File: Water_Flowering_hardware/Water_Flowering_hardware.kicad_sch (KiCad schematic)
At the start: 14 parts, among them J1 Water_Level_Sensor_Module, J2 Soil_Moisture_Sensor_Module, J3 Conn_01x02, J4 Power Jack, K1 Relay_SPDT, Q1 MMBT5550L, U1 CD74HC4067SM, U2 WeMos_D1_mini

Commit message: Fix: 修正JACK的VIN和GND腳位和走線和修正5V的走線
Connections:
- net GND: now also J4.2 (Pin_2); no longer J4.1 (Pin_1)
- net VIN: now also J4.1 (Pin_1); no longer J4.2 (Pin_2)
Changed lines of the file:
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@@
 	)
 	(label "VIN"
-		(at 114.9604 169.4942 180)
+		(at 120.65 166.37 180)
 		(fields_autoplaced yes)
 		(effects
@@
 		)
 	)
+	(label "GND"
+		(at 120.65 171.45 180)
+		(fields_autoplaced yes)
+		(effects
+			(font
+				(size 1.27 1.27)
+			)
+			(justify right bottom)
+		)
+	)
 	(label "Soil_D0"
 		(at 168.91 88.9 0)
@@
 		)
 	)
-	(label "GND"
-		(at 114.9604 172.0342 180)
-		(fields_autoplaced yes)
-		(effects
-			(font
-				(size 1.27 1.27)
-			)
-			(justify right bottom)
-		)
-	)
 	(label "W0"
 		(at 168.91 91.44 0)
@@
 	)
 	(label "GND"
-		(at 114.9604 166.9542 180)
+		(at 120.65 168.91 180)
 		(fields_autoplaced yes)
 		(effects
@@
 			)
 			(justify right bottom)
+		)
+	)
+	(symbol
+		(lib_id "Connector:Conn_01x03_Socket")
+		(at 125.73 168.91 0)
+		(unit 1)
+		(exclude_from_sim no)
+		(in_bom yes)
+		(on_board yes)
+		(dnp no)
+		(property "Reference" "J4"
+			(at 121.92 162.56 0)
+			(effects
+				(font
+					(size 1.27 1.27)
+				)
+				(justify left)
+			)
+		)
+		(property "Value" "Power Jack"
+			(at 114.3 173.99 0)
+			(effects
+				(font
+					(size 1.27 1.27)
+				)
+				(justify left)
+			)
+		)
+		(property "Footprint" "Connector_BarrelJack:BarrelJack_GCT_DCJ200-10-A_Horizontal"
+			(at 125.73 168.91 0)
+			(effects
+				(font
+					(size 1.27 1.27)
+				)
+				(hide yes)
+			)
+		)
+		(property "Datasheet" "~"
+			(at 125.73 168.91 0)
+			(effects
+				(font
+					(size 1.27 1.27)
+				)
+				(hide yes)
+			)
+		)
+		(property "Description" ""
+			(at 125.73 168.91 0)
+			(effects
+				(font
+					(size 1.27 1.27)
+				)
+				(hide yes)
+			)
+		)
+		(pin "1"
+		)
+		(pin "2"
+		)
+		(pin "3"
+		)
+		(instances
+			(project "Water_Flowering_hardware"
+				(path "/2430d23c-7a32-4c0f-92aa-bc816bceade1"
+					(reference "J4")
+					(unit 1)
+				)
+			)
 		)
 	)
@@
 					(unit 1)
 				)
-			)
-		)
-	)
-	(symbol
-		(lib_id "Connector:Conn_01x03_Socket")
-		(at 120.0404 169.4942 0)
-		(unit 1)
-		(exclude_from_sim no)
-		(in_bom yes)
-		(on_board yes)
-		(dnp no)
-		(property "Reference" "J4"
-			(at 116.2304 163.1442 0)
-			(effects
-				(font
-					(size 1.27 1.27)
-				)
-				(justify left)
-			)
-		)
-		(property "Value" "Power Jack"
-			(at 108.6104 174.5742 0)
-			(effects
-				(font
-					(size 1.27 1.27)
-				)
-				(justify left)
-			)
-		)
-		(property "Footprint" "Connector_BarrelJack:BarrelJack_GCT_DCJ200-10-A_Horizontal"
-			(at 120.0404 169.4942 0)
-			(effects
-				(font
-					(size 1.27 1.27)
-				)
-				(hide yes)
-			)
-		)
-		(property "Datasheet" "~"
-			(at 120.0404 169.4942 0)
-			(effects
-				(font
-					(size 1.27 1.27)
-				)
-				(hide yes)
-			)
-		)
-		(property "Description" ""
-			(at 120.0404 169.4942 0)
-			(effects
-				(font
-					(size 1.27 1.27)
-				)
-				(hide yes)
-			)
-		)
-		(pin "1"
-		)
-		(pin "2"
-		)
-		(pin "3"
-		)
-		(instances
-			(project "Water_Flowering_hardware"
-				(path "/2430d23c-7a32-4c0f-92aa-bc816bceade1"
-					(reference "J4")
-					(unit 1)
-				)

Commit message: Fix: 確認CD74HC4067功能後並修正相對的GPIO腳位
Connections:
- net S4 is gone; now on net S3: U2.13 (SDA/D2)
- net S0: now also U2.4 (SCK/D5); no longer U2.16 (TX)
- net S1: now also U2.5 (MISO/D6); no longer U2.15 (RX)
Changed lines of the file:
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@@
 	)
 	(label "S0"
-		(at 184.15 102.87 180)
-		(fields_autoplaced yes)
-		(effects
-			(font
-				(size 1.27 1.27)
-			)
-			(justify right bottom)
+		(at 204.47 105.41 0)
+		(fields_autoplaced yes)
+		(effects
+			(font
+				(size 1.27 1.27)
+			)
+			(justify left bottom)
 		)
 	)
@@
 		)
 	)
-	(label "S4"
+	(label "S3"
 		(at 204.47 97.79 0)
 		(fields_autoplaced yes)
@@
 	)
 	(label "S1"
-		(at 184.15 100.33 180)
-		(fields_autoplaced yes)
-		(effects
-			(font
-				(size 1.27 1.27)
-			)
-			(justify right bottom)
-		)
-	)
+		(at 204.47 107.95 0)
+		(fields_autoplaced yes)
+		(effects
+			(font
+				(size 1.27 1.27)
+			)
+			(justify left bottom)
+		)
+	)

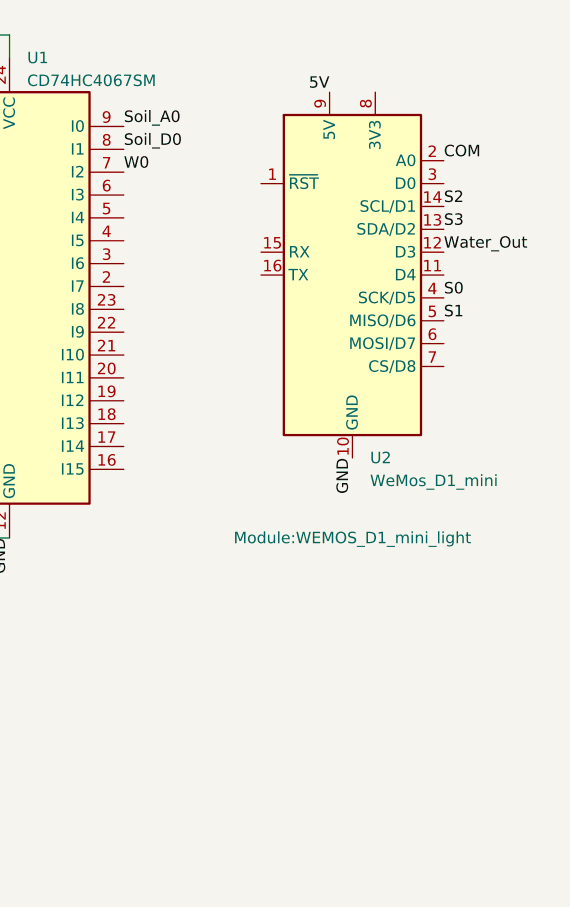
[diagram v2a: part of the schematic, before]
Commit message: Feat: 加入APSTA腳位到D0腳位 - 原本為pull high可進入一種模式(STA或AP)，可透過短路2PIN接地進入另一種模式
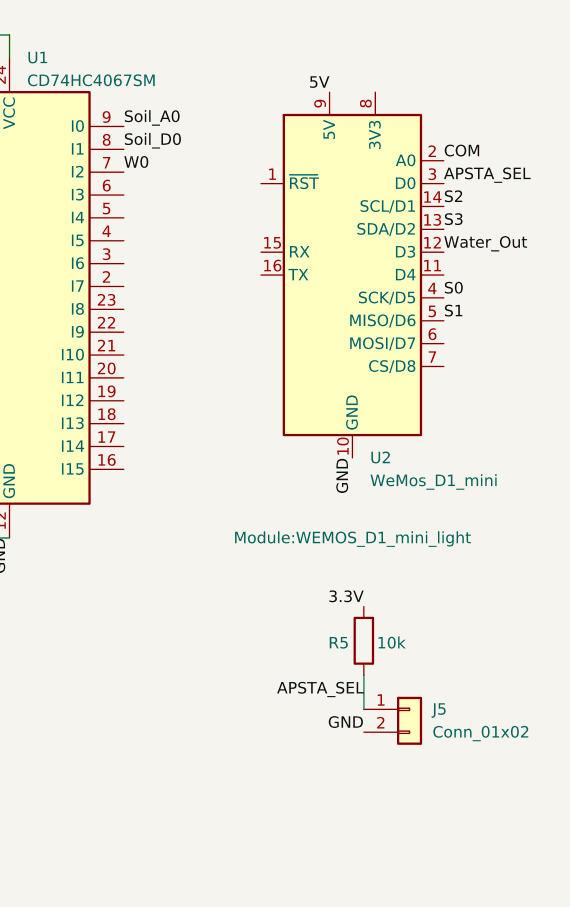
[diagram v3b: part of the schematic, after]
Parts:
- added J5: Conn_01x02, Connector_PinSocket_2.54mm:PinSocket_1x02_P2.54mm_Vertical, symbol Connector_Generic:Conn_01x02
- added R5: 10k, Resistor_SMD:R_0603_1608Metric, symbol Device:R
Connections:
- net 3.3V: now also R5.2
- net GND: now also J5.2 (Pin_2)
- net APSTA_SEL: now reaches U2.3 (D0)
- net APSTA_SEL: now also J5.1 (Pin_1), R5.1
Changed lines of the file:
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@@
+	(wire
+		(pts
+			(xy 195.58 147.32) (xy 195.58 151.13)
+		)
+		(stroke
+			(width 0)
+			(type default)
+		)
+	)
 	(wire
 		(pts
@@
 		)
 	)
+	(label "APSTA_SEL"
+		(at 195.58 149.86 180)
+		(fields_autoplaced yes)
+		(effects
+			(font
+				(size 1.27 1.27)
+			)
+			(justify right bottom)
+		)
+	)
+	(label "GND"
+		(at 195.58 153.67 180)
+		(fields_autoplaced yes)
+		(effects
+			(font
+				(size 1.27 1.27)
+			)
+			(justify right bottom)
+		)
+	)
 	(label "GND"
 		(at 156.21 132.08 270)
@@
 		)
 	)
+	(label "APSTA_SEL"
+		(at 204.47 92.71 0)
+		(fields_autoplaced yes)
+		(effects
+			(font
+				(size 1.27 1.27)
+			)
+			(justify left bottom)
+		)
+	)
 	(label "S3"
 		(at 204.47 97.79 0)
@@
 			)
 			(justify left bottom)
+		)
+	)
+	(label "3.3V"
+		(at 195.58 139.7 180)
+		(fields_autoplaced yes)
+		(effects
+			(font
+				(size 1.27 1.27)
+			)
+			(justify right bottom)
 		)
 	)
@@
 	)
 	(symbol
+		(lib_id "Device:R")
+		(at 195.58 143.51 180)
+		(unit 1)
+		(exclude_from_sim no)
+		(in_bom yes)
+		(on_board yes)
+		(dnp no)
+		(property "Reference" "R5"
+			(at 192.786 143.764 0)
+			(effects
+				(font
+					(size 1.27 1.27)
+				)
+			)
+		)
+		(property "Value" "10k"
+			(at 198.628 143.764 0)
+			(effects
+				(font
+					(size 1.27 1.27)
+				)
+			)
+		)
+		(property "Footprint" "Resistor_SMD:R_0603_1608Metric"
+			(at 197.358 143.51 90)
+			(effects
+				(font
+					(size 1.27 1.27)
+				)
+				(hide yes)
+			)
+		)
+		(property "Datasheet" "~"
+			(at 195.58 143.51 0)
+			(effects
+				(font
+					(size 1.27 1.27)
+				)
+				(hide yes)
+			)
+		)
+		(property "Description" "Resistor"
+			(at 195.58 143.51 0)
+			(effects
+				(font
+					(size 1.27 1.27)
+				)
+				(hide yes)
+			)
+		)
+		(pin "1"
+		)
+		(pin "2"
+		)
+		(instances
+			(project "Water_Flowering_hardware"
+				(path "/2430d23c-7a32-4c0f-92aa-bc816bceade1"
+					(reference "R5")
+					(unit 1)
+				)
+			)
+		)
+	)
+	(symbol
 		(lib_id "Device:D")
 		(at 54.61 52.07 270)
@@
 					(unit 1)
 				)
+			)
+		)
+	)
+	(symbol
+		(lib_id "Connector_Generic:Conn_01x02")
+		(at 200.66 151.13 0)
+		(unit 1)
+		(exclude_from_sim no)
+		(in_bom yes)
+		(on_board yes)
+		(dnp no)
+		(fields_autoplaced yes)
+		(property "Reference" "J5"
+			(at 203.2 151.1299 0)
+			(effects
+				(font
+					(size 1.27 1.27)
+				)
+				(justify left)
+			)
+		)
+		(property "Value" "Conn_01x02"
+			(at 203.2 153.6699 0)
+			(effects
+				(font
+					(size 1.27 1.27)
+				)
+				(justify left)
+			)
+		)
+		(property "Footprint" "Connector_PinSocket_2.54mm:PinSocket_1x02_P2.54mm_Vertical"
+			(at 200.66 151.13 0)
+			(effects
+				(font
+					(size 1.27 1.27)
+				)
+				(hide yes)
+			)
+		)
+		(property "Datasheet" "~"
+			(at 200.66 151.13 0)
+			(effects
+				(font
+					(size 1.27 1.27)
+				)
+				(hide yes)
+			)
+		)
+		(property "Description" "Generic connector, single row, 01x02, script generated (kicad-library-utils/schlib/autogen/connector/)"
+			(at 200.66 151.13 0)
+			(effects
+				(font
+					(size 1.27 1.27)
+				)
+				(hide yes)
+			)
+		)
+		(pin "2"
+		)
+		(pin "1"
+		)
+		(instances
+			(project "Water_Flowering_hardware"
+				(path "/2430d23c-7a32-4c0f-92aa-bc816bceade1"
+					(reference "J5")
+					(unit 1)
+				)

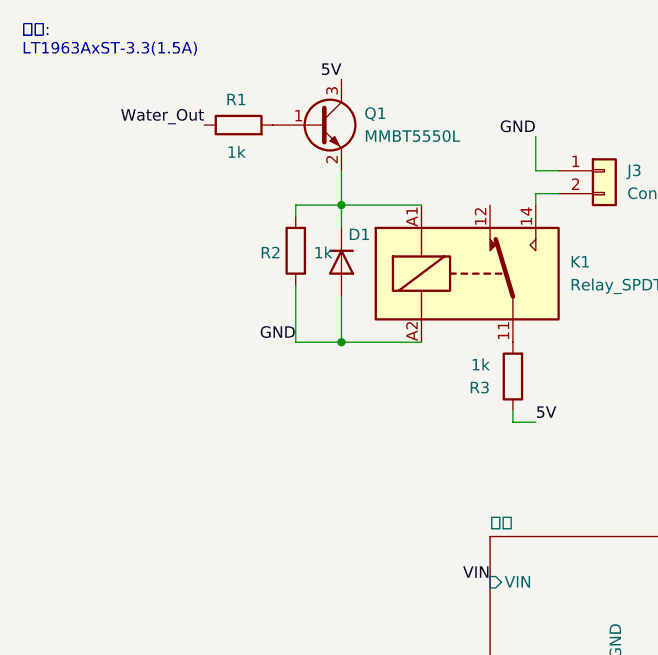
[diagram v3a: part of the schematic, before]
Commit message: Fix: 修正繼電器控制電路 - 加入準位轉換電路(3.3V-5V) - 修正繼電器控制腳位 - 結合準位轉換電路以及用5V輸出準位控制繼電器電路
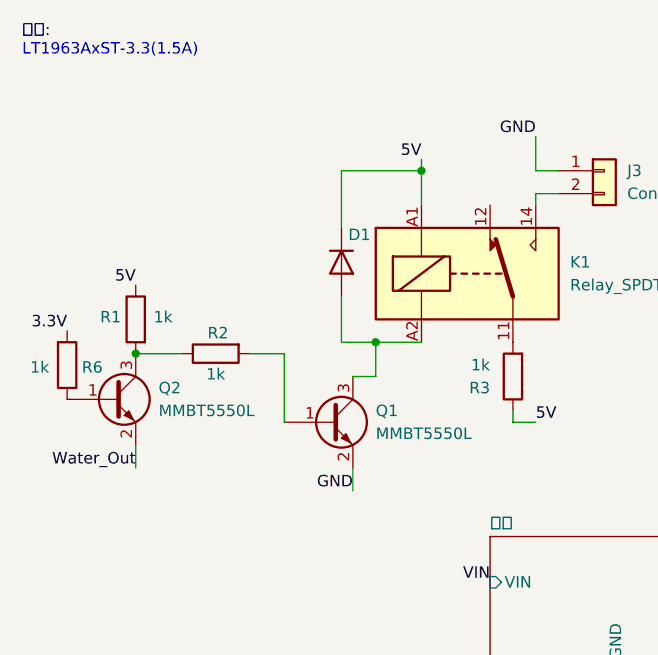
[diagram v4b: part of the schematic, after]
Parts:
- added Q2: MMBT5550L, Package_TO_SOT_SMD:SOT-23, symbol Transistor_BJT:MMBT5550L
- added R6: 1k, Resistor_SMD:R_0603_1608Metric, symbol Device:R
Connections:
- net 3.3V: now also R6.2
- net 5V: now also D1.1 (K), K1.A1, R1.1; no longer Q1.3 (C)
- net GND: now also Q1.2 (E); no longer D1.2 (A), K1.A2, R2.1
- net Water_Out: now also Q2.2 (E); no longer R1.1
- net at R1.2: now also R2.1, Q2.3 (C); no longer Q1.1 (B)
- new net: Q1.1 (B), R2.2
- new net: D1.2 (A), K1.A2, Q1.3 (C)
- new net: Q2.1 (B), R6.1
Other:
- moved on the sheet: Q1, R1

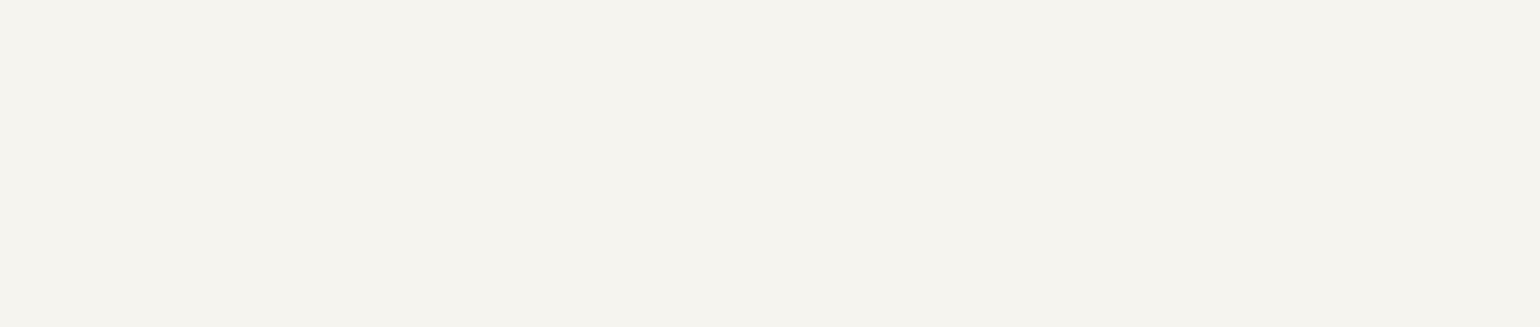
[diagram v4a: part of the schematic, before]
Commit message: Docs: 在原理圖加入準位轉換和繼電器控制電路
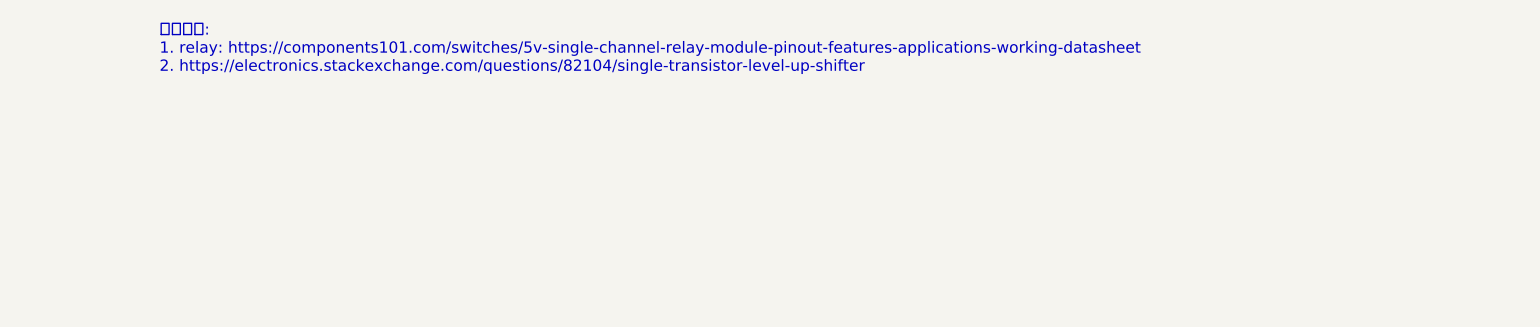
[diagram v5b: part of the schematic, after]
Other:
- note added: "參考資料: 1. relay: https://components101.com/switches/5v-single-channel-relay-module-pinout-features-applications-working-datasheet 2. https://electronics.stackexchange.com/questions/82104/single-transistor-level-up-shifter"
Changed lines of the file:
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@@
+		)
+	)
+	(text "參考資料:\n1. relay: https://components101.com/switches/5v-single-channel-relay-module-pinout-features-applications-working-datasheet\n2. https://electronics.stackexchange.com/questions/82104/single-transistor-level-up-shifter"
+		(exclude_from_sim no)
+		(at 146.304 17.272 0)
+		(effects
+			(font
+				(size 1.27 1.27)
+			)
+			(justify left)
 		)
 	)
